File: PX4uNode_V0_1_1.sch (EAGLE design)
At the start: 130 parts, among them M3_MOUNT1101 MOUNT-HOLE3.1MM, M3_MOUNT1102 MOUNT-HOLE3.1MM, M3_MOUNT1103 MOUNT-HOLE3.1MM, M3_MOUNT1104 MOUNT-HOLE3.1MM, U101 STM32F4X7VX, U401 MAX3051, U402 MAX3051, X101 3.2x2.5 mm / 24 MHz / 15 ppm

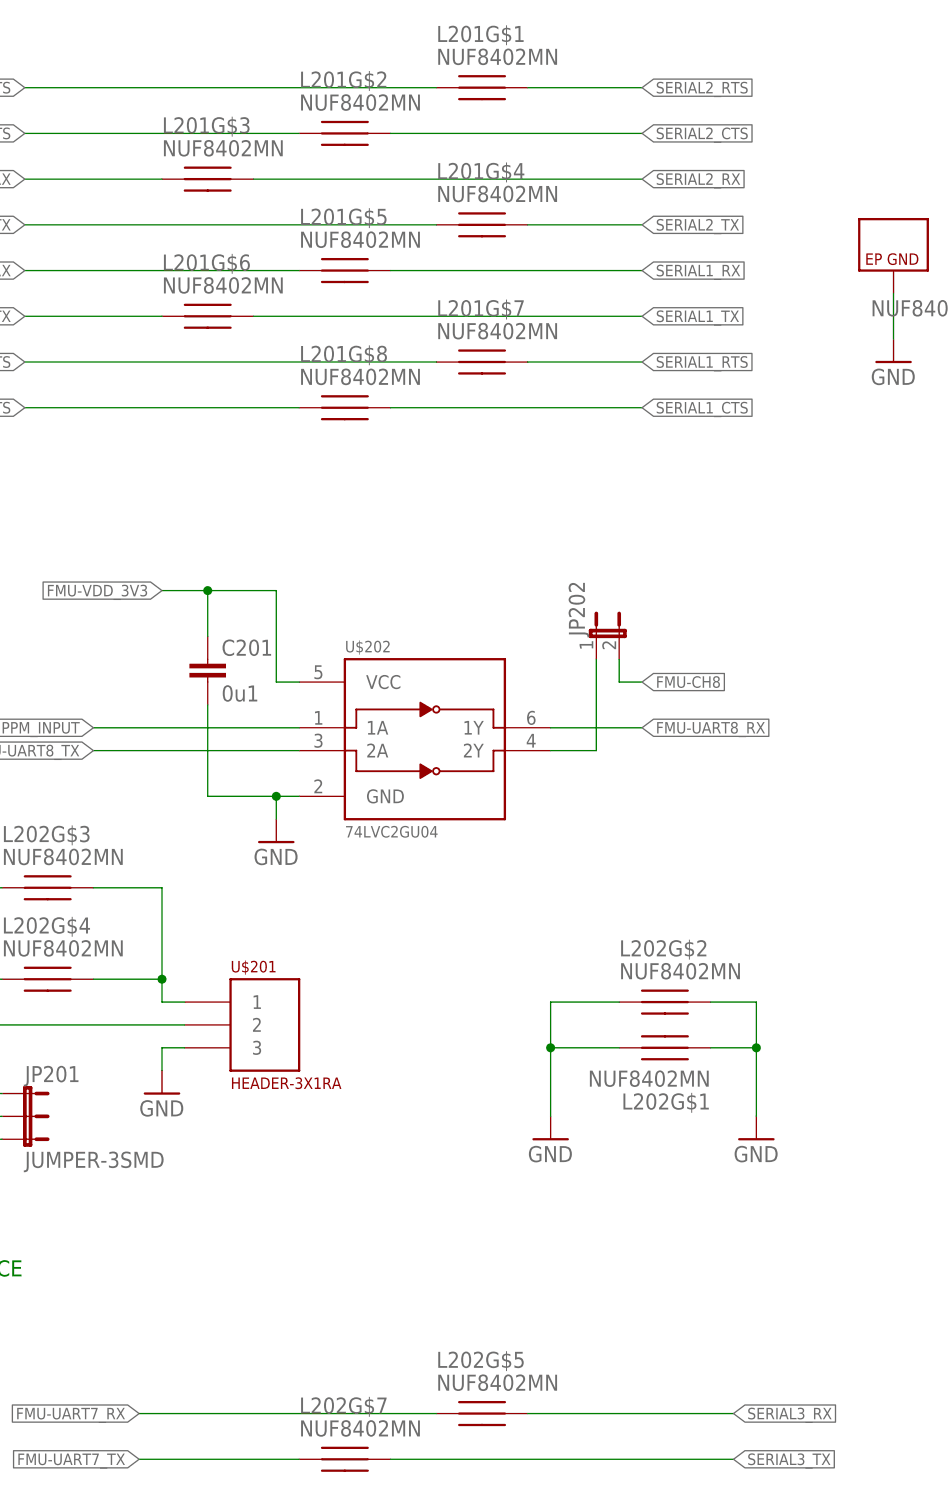
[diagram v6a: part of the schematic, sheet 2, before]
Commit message: Layout UART 1&2
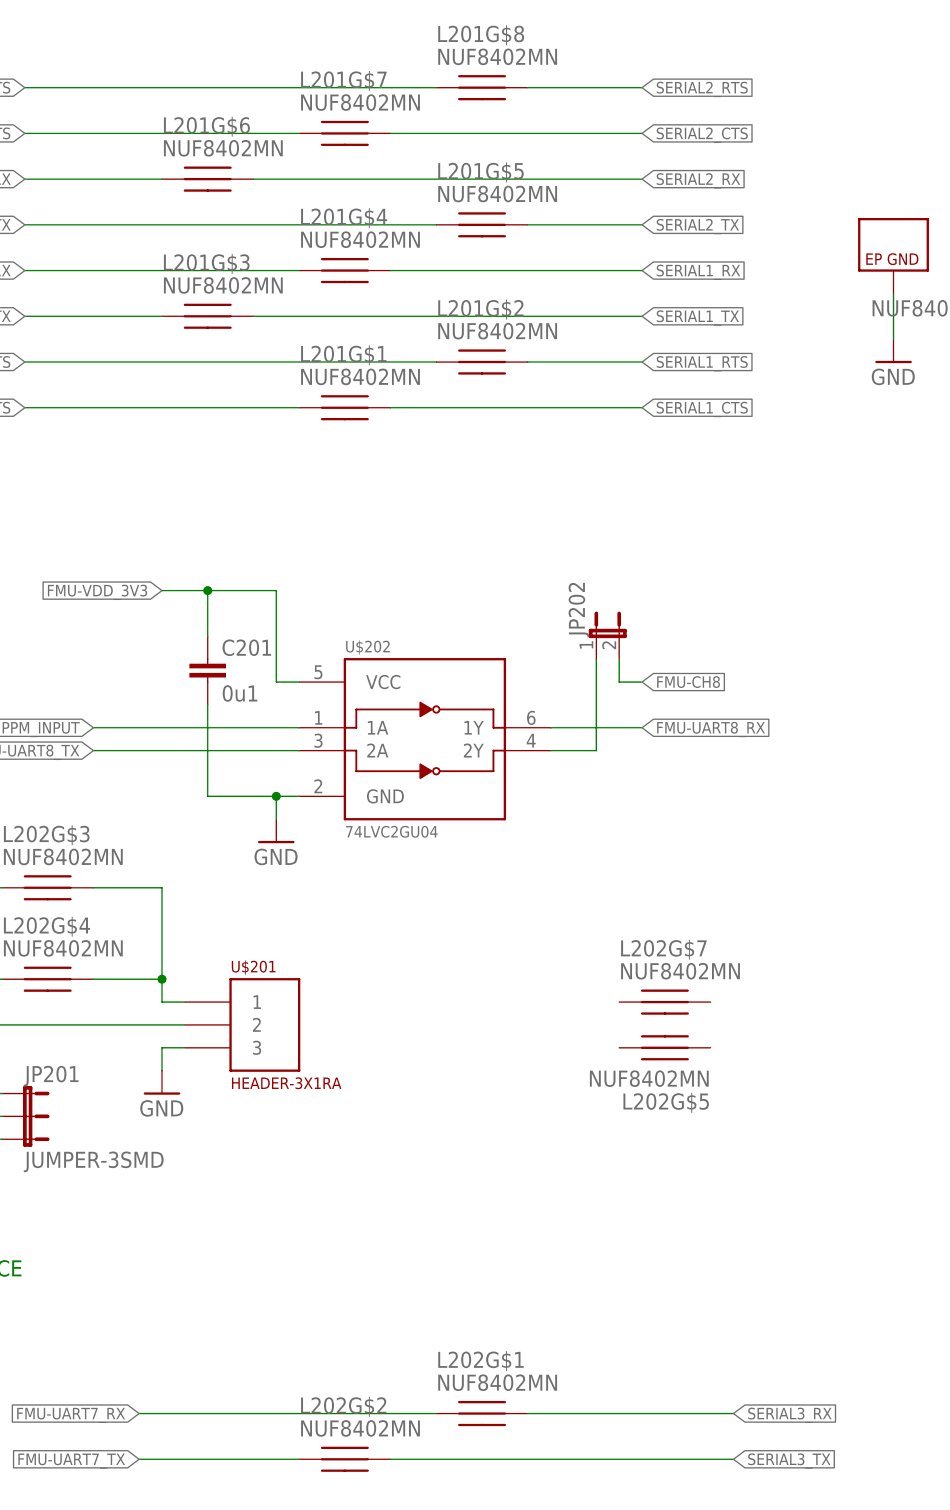
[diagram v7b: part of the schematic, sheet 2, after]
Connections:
- net FMU-UART7_RX: now also L202G$1.P$1; no longer L202G$5.P$1
- net FMU-UART7_TX: now also L202G$2.P$1; no longer L202G$7.P$1
- net FMU-USART2_CTS: now also L201G$1.P$1; no longer L201G$8.P$1
- net FMU-USART2_RTS: now also L201G$2.P$1; no longer L201G$7.P$1
- net FMU-USART2_RX: now also L201G$4.P$1; no longer L201G$5.P$1
- net FMU-USART2_TX: now also L201G$3.P$1; no longer L201G$6.P$1
- net FMU-USART3_CTS: now also L201G$7.P$1; no longer L201G$2.P$1
- net FMU-USART3_RTS: now also L201G$8.P$1; no longer L201G$1.P$1
- net FMU-USART3_RX: now also L201G$6.P$1; no longer L201G$3.P$1
- net FMU-USART3_TX: now also L201G$5.P$1; no longer L201G$4.P$1
- net GND: no longer L202G$1.P$1, L202G$1.P$2, L202G$2.P$1, L202G$2.P$2
- net SERIAL1_CTS: now also L201G$1.P$2; no longer L201G$8.P$2
- net SERIAL1_RTS: now also L201G$2.P$2; no longer L201G$7.P$2
- net SERIAL1_RX: now also L201G$4.P$2; no longer L201G$5.P$2
- net SERIAL1_TX: now also L201G$3.P$2; no longer L201G$6.P$2
- net SERIAL2_CTS: now also L201G$7.P$2; no longer L201G$2.P$2
- net SERIAL2_RTS: now also L201G$8.P$2; no longer L201G$1.P$2
- net SERIAL2_RX: now also L201G$6.P$2; no longer L201G$3.P$2
- net SERIAL2_TX: now also L201G$5.P$2; no longer L201G$4.P$2
- net SERIAL3_RX: now also L202G$1.P$2; no longer L202G$5.P$2
- net SERIAL3_TX: now also L202G$2.P$2; no longer L202G$7.P$2
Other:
- moved on the sheet: L201G$1, L201G$2, L201G$3, L201G$4, L201G$5, L201G$6, L201G$7, L201G$8, L202G$1, L202G$2, L202G$5, L202G$7
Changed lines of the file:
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@@
 <attribute name="BOM" value="EXCLUDE"/>
 </part>
-<part name="GND19" library="pixhawk2" deviceset="GND" device=""/>
-<part name="GND22" library="pixhawk2" deviceset="GND" device=""/>
 <part name="JP1001" library="SparkFun-Connectors" deviceset="M01" device="SMD-4.5X1.5">
 <attribute name="BOM" value="EXCLUDE"/>
@@
 <attribute name="PARTNO" x="210.82" y="78.74" size="1.778" layer="96" display="off"/>
 </instance>
-<instance part="L201" gate="G$1" x="99.06" y="165.1"/>
-<instance part="L201" gate="G$2" x="83.82" y="160.02"/>
-<instance part="L201" gate="G$3" x="68.58" y="154.94"/>
-<instance part="L201" gate="G$4" x="99.06" y="149.86"/>
-<instance part="L201" gate="G$5" x="83.82" y="144.78"/>
-<instance part="L201" gate="G$6" x="68.58" y="139.7"/>
-<instance part="L201" gate="G$7" x="99.06" y="134.62"/>
-<instance part="L201" gate="G$8" x="83.82" y="129.54"/>
+<instance part="L201" gate="G$8" x="99.06" y="165.1"/>
+<instance part="L201" gate="G$7" x="83.82" y="160.02"/>
+<instance part="L201" gate="G$6" x="68.58" y="154.94"/>
+<instance part="L201" gate="G$5" x="99.06" y="149.86"/>
+<instance part="L201" gate="G$4" x="83.82" y="144.78"/>
+<instance part="L201" gate="G$3" x="68.58" y="139.7"/>
+<instance part="L201" gate="G$2" x="99.06" y="134.62"/>
+<instance part="L201" gate="G$1" x="83.82" y="129.54"/>
 <instance part="L201" gate="G$9" x="144.78" y="142.24"/>
 <instance part="GND8" gate="1" x="144.78" y="134.62"/>
 <instance part="L202" gate="G$9" x="20.32" y="20.32"/>
-<instance part="L202" gate="G$5" x="99.06" y="17.78"/>
-<instance part="L202" gate="G$7" x="83.82" y="12.7"/>
+<instance part="L202" gate="G$1" x="99.06" y="17.78"/>
+<instance part="L202" gate="G$2" x="83.82" y="12.7"/>
 <instance part="L202" gate="G$3" x="50.8" y="76.2"/>
 <instance part="L202" gate="G$4" x="50.8" y="66.04"/>
@@
 <instance part="GND46" gate="1" x="63.5" y="53.34"/>
 <instance part="U$201" gate="G$1" x="73.66" y="58.42"/>
-<instance part="L202" gate="G$1" x="119.38" y="58.42" rot="R180"/>
+<instance part="L202" gate="G$5" x="119.38" y="58.42" rot="R180"/>
 <instance part="L202" gate="G$6" x="160.02" y="43.18"/>
-<instance part="L202" gate="G$2" x="119.38" y="63.5"/>
+<instance part="L202" gate="G$7" x="119.38" y="63.5"/>
 <instance part="L202" gate="G$8" x="170.18" y="35.56"/>
 <instance part="U$202" gate="G$1" x="91.44" y="91.44">
@@
 <attribute name="BOM" x="111.76" y="104.14" size="1.778" layer="96" display="off"/>
 </instance>
-<instance part="GND19" gate="1" x="106.68" y="48.26"/>
-<instance part="GND22" gate="1" x="129.54" y="48.26"/>
 <instance part="JP12" gate="G$1" x="220.98" y="147.32"/>
 <instance part="JP1" gate="G$1" x="220.98" y="109.22"/>
@@
 <segment>
 <label x="116.84" y="129.54" size="1.27" layer="95" xref="yes"/>
-<pinref part="L201" gate="G$8" pin="P$2"/>
+<pinref part="L201" gate="G$1" pin="P$2"/>
 <wire x1="116.84" y1="129.54" x2="88.9" y2="129.54" width="0.1524" layer="91"/>
 </segment>
@@
 <segment>
 <label x="116.84" y="134.62" size="1.27" layer="95" xref="yes"/>
-<pinref part="L201" gate="G$7" pin="P$2"/>
+<pinref part="L201" gate="G$2" pin="P$2"/>
 <wire x1="116.84" y1="134.62" x2="104.14" y2="134.62" width="0.1524" layer="91"/>
 </segment>
@@
 <segment>
 <label x="116.84" y="149.86" size="1.27" layer="95" xref="yes"/>
-<pinref part="L201" gate="G$4" pin="P$2"/>
+<pinref part="L201" gate="G$5" pin="P$2"/>
 <wire x1="116.84" y1="149.86" x2="104.14" y2="149.86" width="0.1524" layer="91"/>
 </segment>
@@
 <segment>
 <label x="116.84" y="160.02" size="1.27" layer="95" xref="yes"/>
-<pinref part="L201" gate="G$2" pin="P$2"/>
+<pinref part="L201" gate="G$7" pin="P$2"/>
 <wire x1="116.84" y1="160.02" x2="88.9" y2="160.02" width="0.1524" layer="91"/>
 </segment>
@@
 <segment>
 <label x="116.84" y="165.1" size="1.27" layer="95" xref="yes"/>
-<pinref part="L201" gate="G$1" pin="P$2"/>
+<pinref part="L201" gate="G$8" pin="P$2"/>
 <wire x1="116.84" y1="165.1" x2="104.14" y2="165.1" width="0.1524" layer="91"/>
 </segment>
@@
 <segment>
 <label x="116.84" y="139.7" size="1.27" layer="95" xref="yes"/>
-<pinref part="L201" gate="G$6" pin="P$2"/>
+<pinref part="L201" gate="G$3" pin="P$2"/>
 <wire x1="116.84" y1="139.7" x2="73.66" y2="139.7" width="0.1524" layer="91"/>
 </segment>
@@
 <segment>
 <label x="116.84" y="144.78" size="1.27" layer="95" xref="yes"/>
-<pinref part="L201" gate="G$5" pin="P$2"/>
+<pinref part="L201" gate="G$4" pin="P$2"/>
 <wire x1="116.84" y1="144.78" x2="88.9" y2="144.78" width="0.1524" layer="91"/>
 </segment>
@@
 <segment>
 <label x="116.84" y="154.94" size="1.27" layer="95" xref="yes"/>
-<pinref part="L201" gate="G$3" pin="P$2"/>
+<pinref part="L201" gate="G$6" pin="P$2"/>
 <wire x1="116.84" y1="154.94" x2="73.66" y2="154.94" width="0.1524" layer="91"/>
 </segment>
@@
 <segment>
 <label x="127" y="12.7" size="1.27" layer="95" xref="yes"/>
-<pinref part="L202" gate="G$7" pin="P$2"/>
+<pinref part="L202" gate="G$2" pin="P$2"/>
 <wire x1="127" y1="12.7" x2="88.9" y2="12.7" width="0.1524" layer="91"/>
 </segment>
@@
 <segment>
 <label x="127" y="17.78" size="1.27" layer="95" xref="yes"/>
-<pinref part="L202" gate="G$5" pin="P$2"/>
+<pinref part="L202" gate="G$1" pin="P$2"/>
 <wire x1="127" y1="17.78" x2="104.14" y2="17.78" width="0.1524" layer="91"/>
 </segment>
@@
 <segment>
 <label x="48.26" y="144.78" size="1.27" layer="95" rot="R180" xref="yes"/>
+<pinref part="L201" gate="G$4" pin="P$1"/>
+<wire x1="78.74" y1="144.78" x2="48.26" y2="144.78" width="0.1524" layer="91"/>
+</segment>
+</net>
+<net name="FMU-USART2_RTS" class="0">
+<segment>
+<label x="48.26" y="134.62" size="1.27" layer="95" rot="R180" xref="yes"/>
+<pinref part="L201" gate="G$2" pin="P$1"/>
+<wire x1="93.98" y1="134.62" x2="48.26" y2="134.62" width="0.1524" layer="91"/>
+</segment>
+</net>
+<net name="FMU-USART3_TX" class="0">
+<segment>
+<label x="48.26" y="149.86" size="1.27" layer="95" rot="R180" xref="yes"/>
 <pinref part="L201" gate="G$5" pin="P$1"/>
-<wire x1="78.74" y1="144.78" x2="48.26" y2="144.78" width="0.1524" layer="91"/>
-</segment>
-</net>
-<net name="FMU-USART2_RTS" class="0">
-<segment>
-<label x="48.26" y="134.62" size="1.27" layer="95" rot="R180" xref="yes"/>
-<pinref part="L201" gate="G$7" pin="P$1"/>
-<wire x1="93.98" y1="134.62" x2="48.26" y2="134.62" width="0.1524" layer="91"/>
-</segment>
-</net>
-<net name="FMU-USART3_TX" class="0">
-<segment>
-<label x="48.26" y="149.86" size="1.27" layer="95" rot="R180" xref="yes"/>
-<pinref part="L201" gate="G$4" pin="P$1"/>
 <wire x1="48.26" y1="149.86" x2="93.98" y2="149.86" width="0.1524" layer="91"/>
 </segment>
@@
 <segment>
 <label x="48.26" y="154.94" size="1.27" layer="95" rot="R180" xref="yes"/>
-<pinref part="L201" gate="G$3" pin="P$1"/>
+<pinref part="L201" gate="G$6" pin="P$1"/>
 <wire x1="63.5" y1="154.94" x2="48.26" y2="154.94" width="0.1524" layer="91"/>
 </segment>
@@
 <label x="48.26" y="160.02" size="1.27" layer="95" rot="R180" xref="yes"/>
 <wire x1="48.26" y1="160.02" x2="78.74" y2="160.02" width="0.1524" layer="91"/>
-<pinref part="L201" gate="G$2" pin="P$1"/>
+<pinref part="L201" gate="G$7" pin="P$1"/>
 </segment>
 </net>
@@
 <segment>
 <label x="48.26" y="165.1" size="1.27" layer="95" rot="R180" xref="yes"/>
-<pinref part="L201" gate="G$1" pin="P$1"/>
+<pinref part="L201" gate="G$8" pin="P$1"/>
 <wire x1="93.98" y1="165.1" x2="48.26" y2="165.1" width="0.1524" layer="91"/>
 </segment>
@@
 <segment>
 <label x="48.26" y="139.7" size="1.27" layer="95" rot="R180" xref="yes"/>
-<pinref part="L201" gate="G$6" pin="P$1"/>
+<pinref part="L201" gate="G$3" pin="P$1"/>
 <wire x1="48.26" y1="139.7" x2="63.5" y2="139.7" width="0.1524" layer="91"/>
 </segment>
@@
 <segment>
 <label x="48.26" y="129.54" size="1.27" layer="95" rot="R180" xref="yes"/>
-<pinref part="L201" gate="G$8" pin="P$1"/>
+<pinref part="L201" gate="G$1" pin="P$1"/>
 <wire x1="48.26" y1="129.54" x2="78.74" y2="129.54" width="0.1524" layer="91"/>
 </segment>
@@
 <junction x="76.2" y="86.36"/>
 </segment>
-<segment>
-<wire x1="114.3" y1="63.5" x2="106.68" y2="63.5" width="0.1524" layer="91"/>
-<pinref part="GND19" gate="1" pin="GND"/>
-<wire x1="106.68" y1="63.5" x2="106.68" y2="58.42" width="0.1524" layer="91"/>
-<pinref part="L202" gate="G$1" pin="P$2"/>
-<wire x1="106.68" y1="58.42" x2="106.68" y2="50.8" width="0.1524" layer="91"/>
-<wire x1="114.3" y1="58.42" x2="106.68" y2="58.42" width="0.1524" layer="91"/>
-<junction x="106.68" y="58.42"/>
-<pinref part="L202" gate="G$2" pin="P$1"/>
-</segment>
-<segment>
-<pinref part="GND22" gate="1" pin="GND"/>
-<wire x1="129.54" y1="50.8" x2="129.54" y2="58.42" width="0.1524" layer="91"/>
-<pinref part="L202" gate="G$2" pin="P$2"/>
-<wire x1="129.54" y1="58.42" x2="129.54" y2="63.5" width="0.1524" layer="91"/>
-<wire x1="129.54" y1="63.5" x2="124.46" y2="63.5" width="0.1524" layer="91"/>
-<pinref part="L202" gate="G$1" pin="P$1"/>
-<wire x1="124.46" y1="58.42" x2="129.54" y2="58.42" width="0.1524" layer="91"/>
-<junction x="129.54" y="58.42"/>
-</segment>
 </net>
 <net name="VDD_5V_PERIPH" class="1">
@@
 <segment>
 <label x="60.96" y="17.78" size="1.27" layer="95" rot="R180" xref="yes"/>
-<pinref part="L202" gate="G$5" pin="P$1"/>
+<pinref part="L202" gate="G$1" pin="P$1"/>
 <wire x1="60.96" y1="17.78" x2="93.98" y2="17.78" width="0.1524" layer="91"/>
 </segment>
@@
 <segment>
 <label x="60.96" y="12.7" size="1.27" layer="95" rot="R180" xref="yes"/>
-<pinref part="L202" gate="G$7" pin="P$1"/>
+<pinref part="L202" gate="G$2" pin="P$1"/>
 <wire x1="78.74" y1="12.7" x2="60.96" y2="12.7" width="0.1524" layer="91"/>
 </segment>
